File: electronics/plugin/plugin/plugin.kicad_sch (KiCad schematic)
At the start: 12 parts, among them J1 Conn_01x01, J2 Conn_01x01, J3 Conn_01x02, Q2 Q_NMOS_DSG, Y1 Piezo

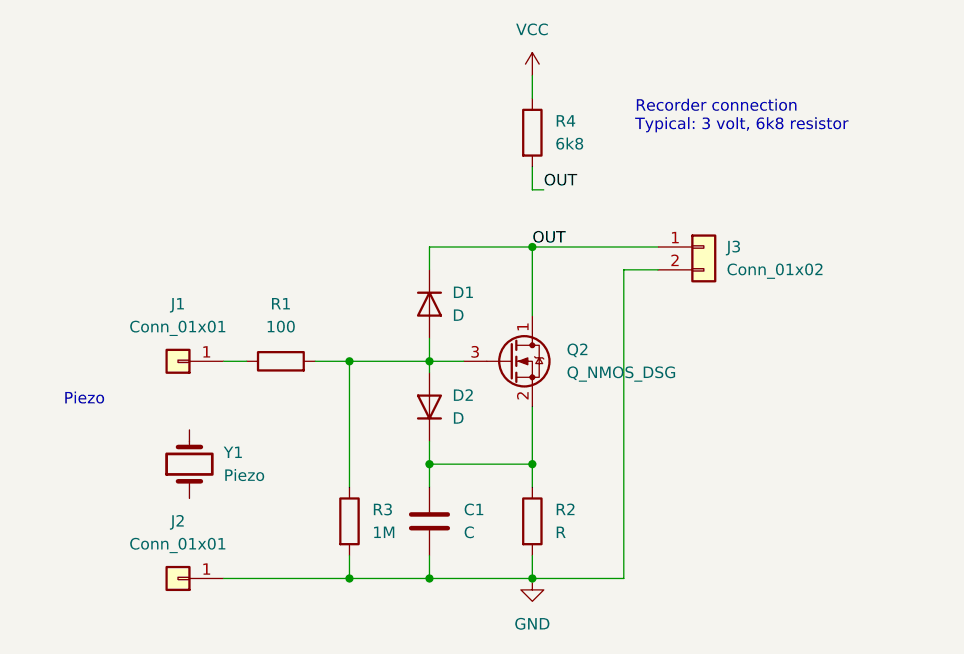
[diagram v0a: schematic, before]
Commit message: plugin: Fix protection, notes on solder test and JFET amp setup
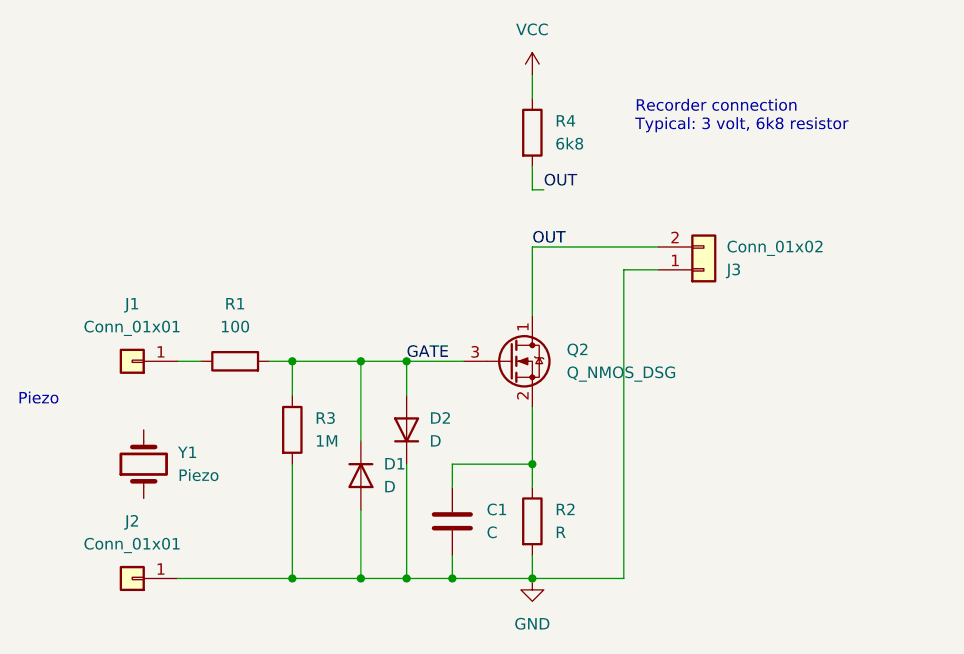
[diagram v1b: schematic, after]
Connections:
- net GND: now also D1.2 (A), D2.1 (K), J3.1 (Pin_1); no longer J3.2 (Pin_2)
- net OUT: now also J3.2 (Pin_2); no longer D1.1 (K), J3.1 (Pin_1)
- net GATE: now reaches D2.2 (A), Q2.3 (G), R1.2, R3.1
- net GATE: now also D1.1 (K); no longer D1.2 (A)
- net at C1.1, Q2.2 (S), R2.1: no longer D2.1 (K)
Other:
- moved on the sheet: C1, D1, D2, J1, J2, R1, R3, Y1
